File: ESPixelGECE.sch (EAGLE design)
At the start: 15 parts, among them Q1 MOSFET-NCHANNEL2N7000

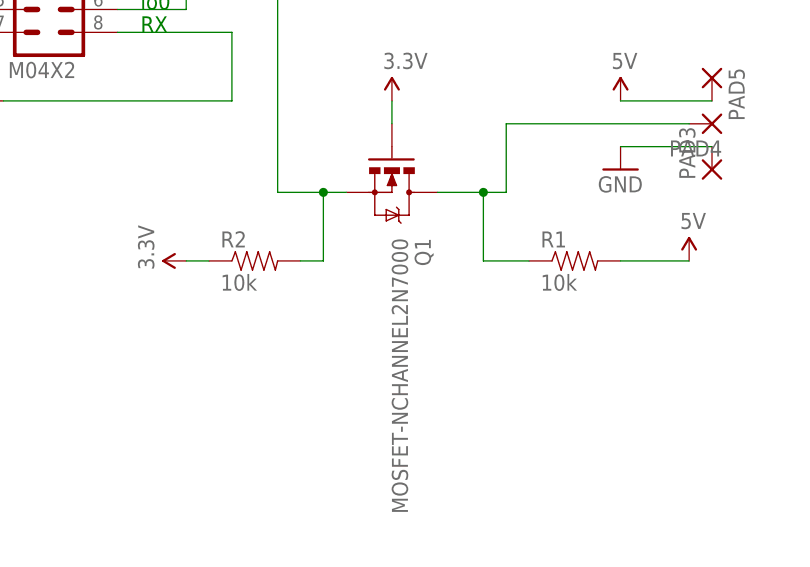
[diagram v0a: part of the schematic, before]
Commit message: Added BOMs, SEEED cam
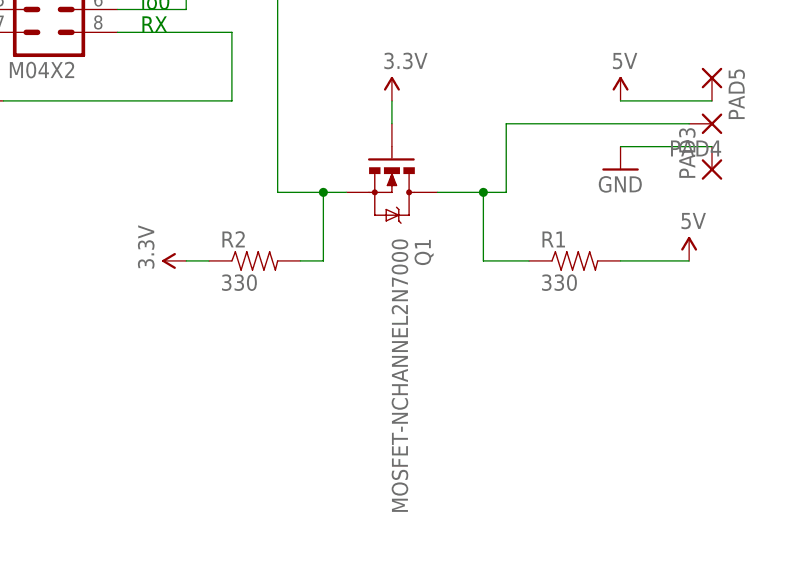
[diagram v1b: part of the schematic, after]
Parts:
- R1, R2: value 10k -> 330
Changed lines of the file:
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@@
 <?xml version="1.0" encoding="utf-8"?>
 <!DOCTYPE eagle SYSTEM "eagle.dtd">
-<eagle version="7.2.0">
+<eagle version="7.4.0">
 <drawing>
 <settings>
@@
 <part name="C2" library="SparkFun-Capacitors" deviceset="CAP_POL" device="PTH2" value="10u"/>
 <part name="SUPPLY2" library="SparkFun-Aesthetics" deviceset="3.3V" device=""/>
-<part name="R1" library="SparkFun-Resistors" deviceset="RESISTOR" device="EZ" value="10k"/>
+<part name="R1" library="SparkFun-Resistors" deviceset="RESISTOR" device="EZ" value="330"/>
 <part name="SUPPLY6" library="SparkFun-Aesthetics" deviceset="5V" device=""/>
 <part name="SUPPLY7" library="SparkFun-Aesthetics" deviceset="5V" device=""/>
@@
 <part name="S1" library="SparkFun-Retired" deviceset="TAC_SWITCH" device="PTH"/>
 <part name="Q1" library="SparkFun-DiscreteSemi" deviceset="MOSFET-NCHANNEL" device="2N7000"/>
-<part name="R2" library="SparkFun-Resistors" deviceset="RESISTOR" device="EZ" value="10k"/>
+<part name="R2" library="SparkFun-Resistors" deviceset="RESISTOR" device="EZ" value="330"/>
 <part name="SUPPLY9" library="SparkFun-Aesthetics" deviceset="3.3V" device=""/>
 <part name="FRAME1" library="frames" deviceset="LETTER_L" device=""/>
